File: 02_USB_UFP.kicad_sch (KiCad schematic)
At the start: 30 parts, among them U2 PI3USB302-Ax, U3 TUSB522Px, U4 TVS2200DRVx

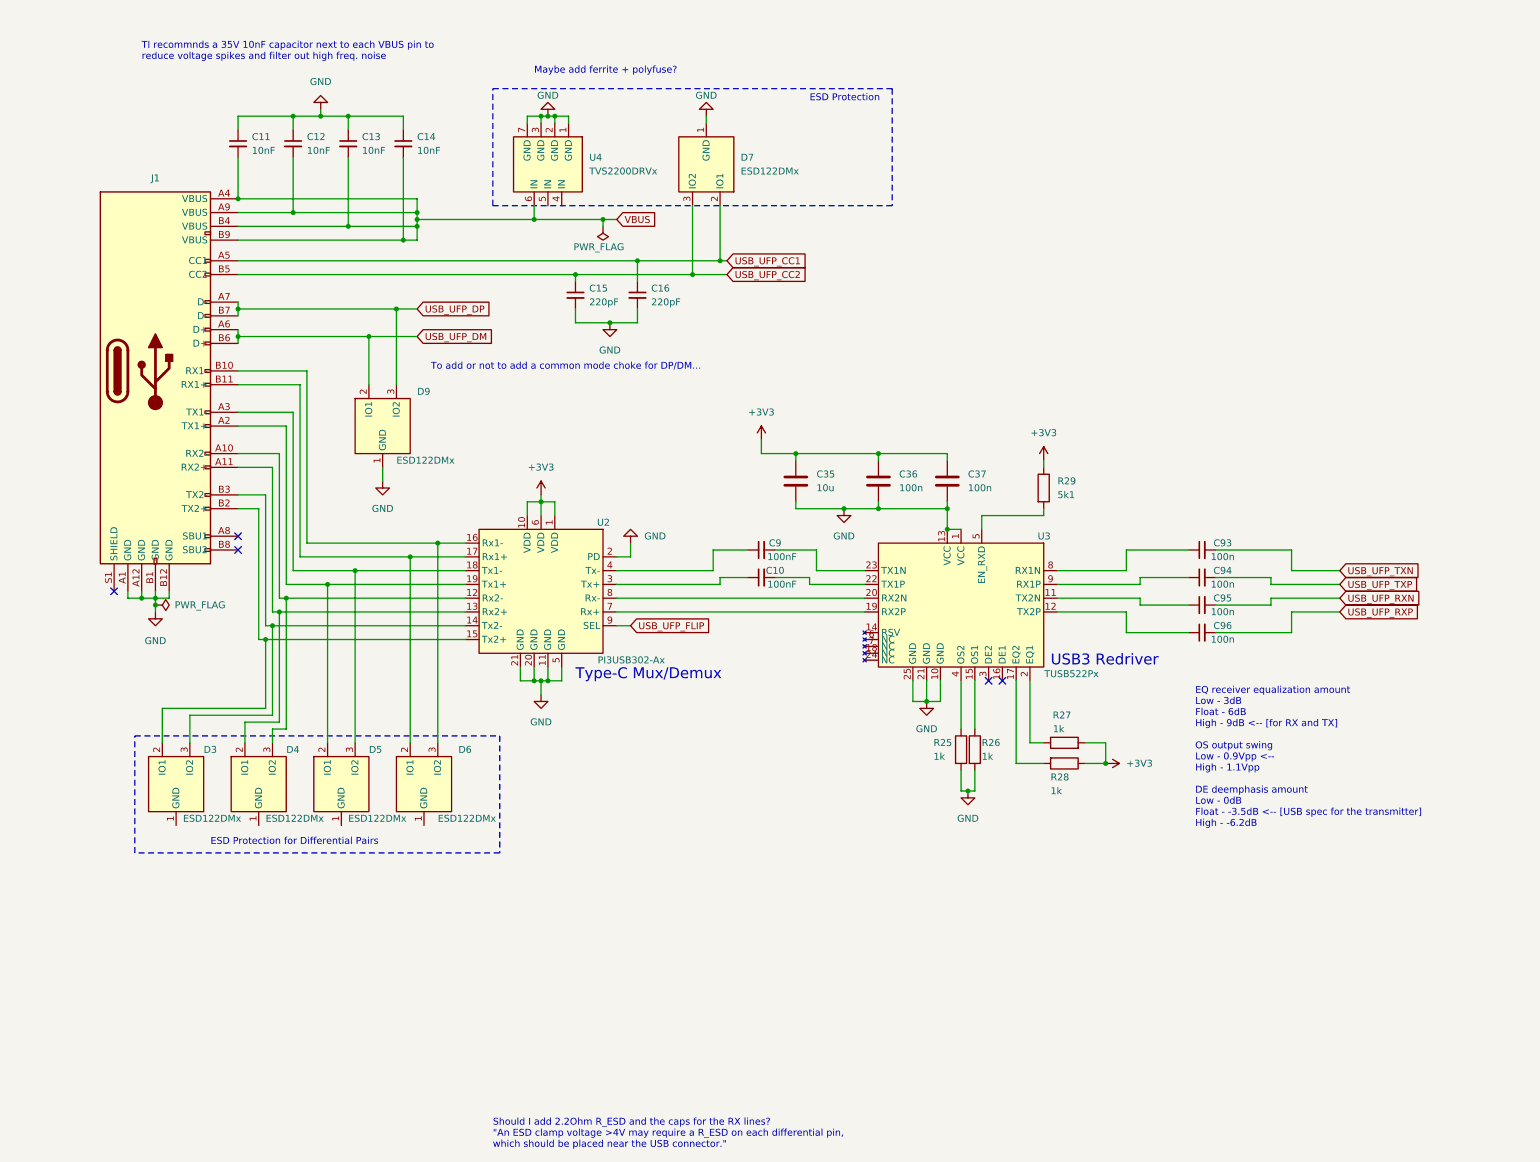
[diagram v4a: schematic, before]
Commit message: finish up schematics and ERC
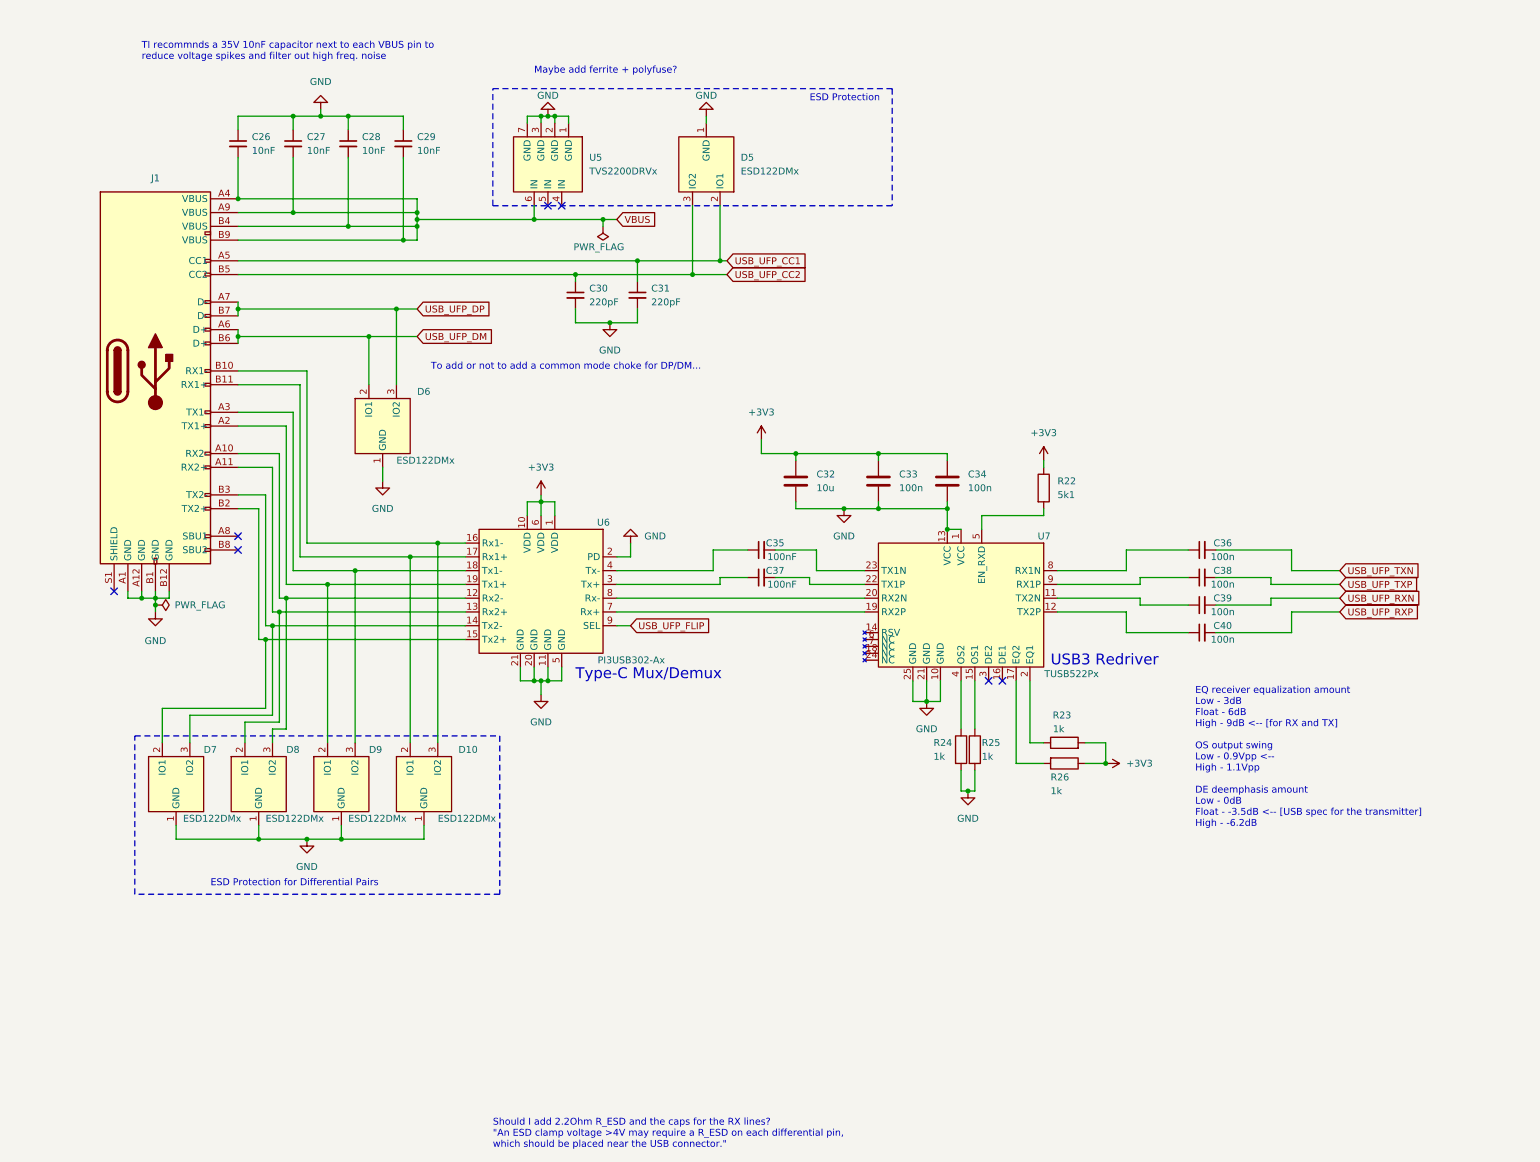
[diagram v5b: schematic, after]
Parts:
- renumbered C11 to C26, C12 to C27, C13 to C28, C14 to C29, C15 to C30, C16 to C31, C35 to C32, C36 to C33, C37 to C34, C9 to C35, C93 to C36, C10 to C37, C94 to C38, C95 to C39, C96 to C40, D6 to D10, D7 to D5, D9 to D6, D3 to D7, D4 to D8, D5 to D9, R29 to R22, R27 to R23, R25 to R24, R26 to R25, R28 to R26, U4 to U5, U2 to U6, U3 to U7
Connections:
- net GND: now also D10.1 (GND), D7.1 (GND), D8.1 (GND), D9.1 (GND)
- no-connect marks 5 -> 7

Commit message: finish setting footprints
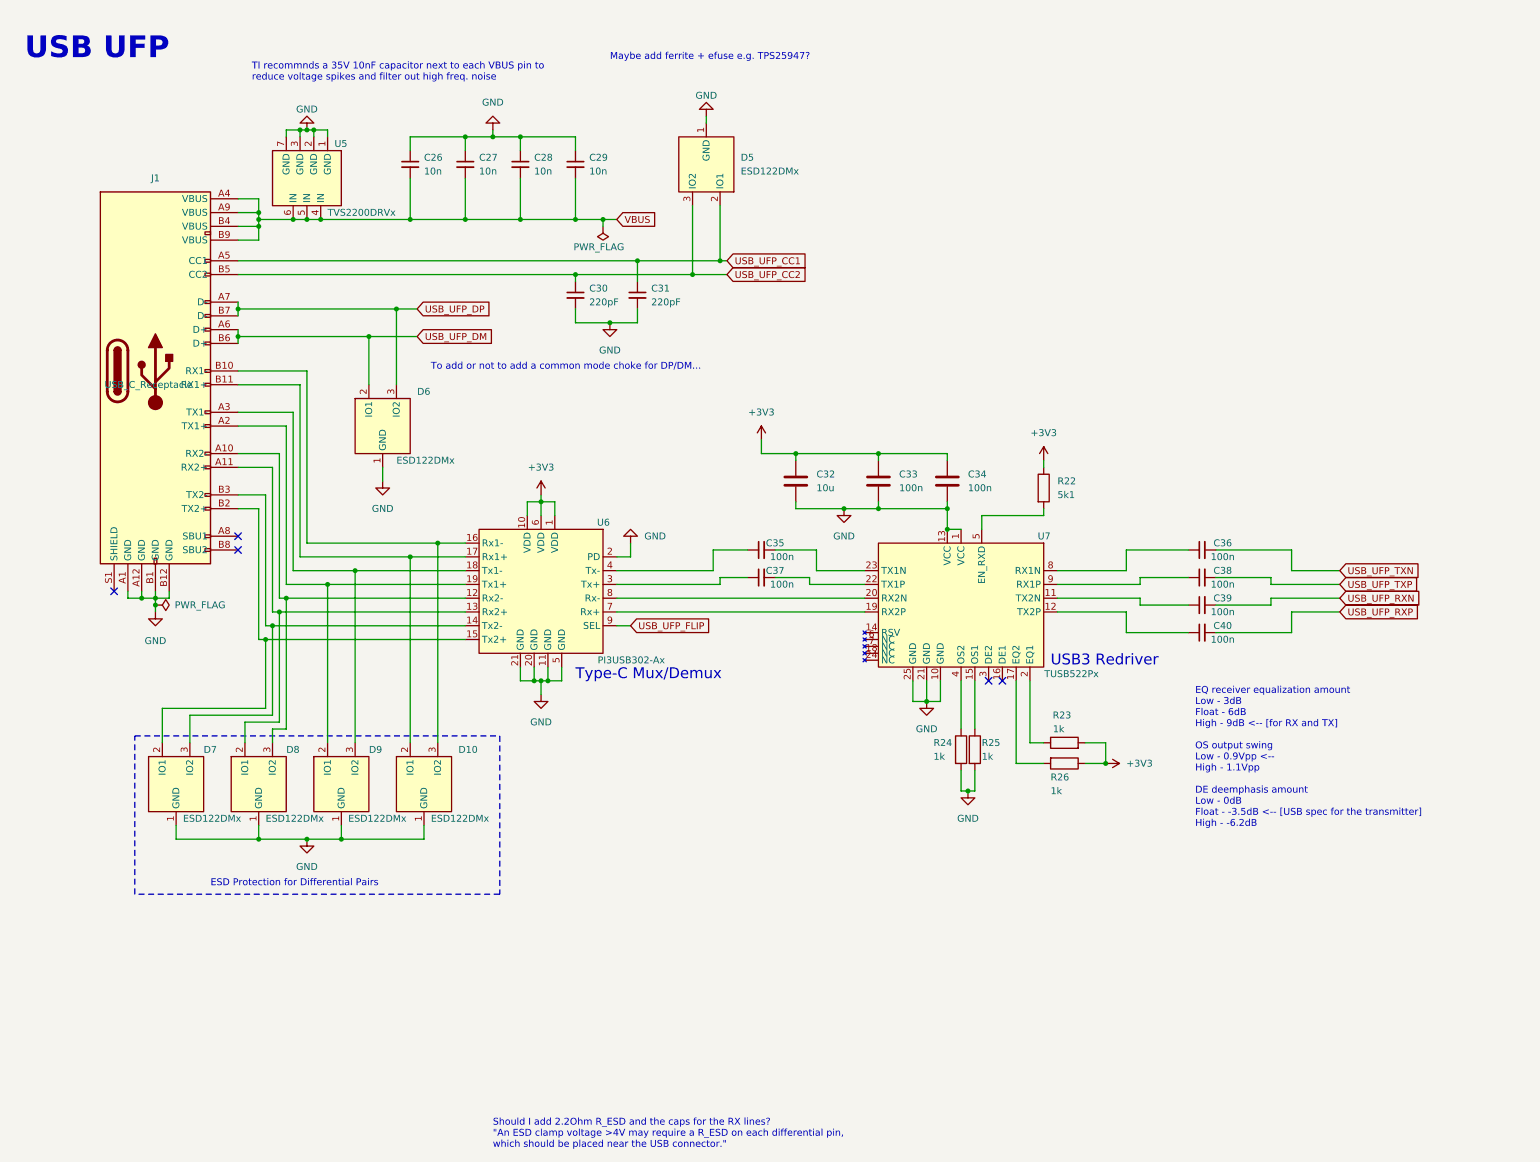
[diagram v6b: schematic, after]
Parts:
- C26, C27, C28, C29: value 10nF -> 10n; footprint (none) -> Capacitor_SMD:C_0603_1608Metric
- C30, C31, C32, C33, C34: footprint (none) -> Capacitor_SMD:C_0603_1608Metric
- C35, C37: value 100nF -> 100n; footprint (none) -> Capacitor_SMD:C_0402_1005Metric
- C36, C38, C39, C40: footprint (none) -> Capacitor_SMD:C_0402_1005Metric
- J1: value ~ -> USB_C_Receptacle; footprint (none) -> CakeUSB:USB_C_Receptacle_GT-USB-7052
- R22, R23, R24, R25, R26: footprint (none) -> Resistor_SMD:R_0603_1608Metric
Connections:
- net VBUS: now also U5.4 (IN), U5.5 (IN)
- no-connect marks 7 -> 5
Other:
- note added: "Maybe add ferrite + efuse e.g. TPS25947?"
- note added: "USB UFP"
- note removed: "ESD Protection"
- note removed: "Maybe add ferrite + polyfuse?"

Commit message: symbol fixes, switch ESD protection for USB datalines
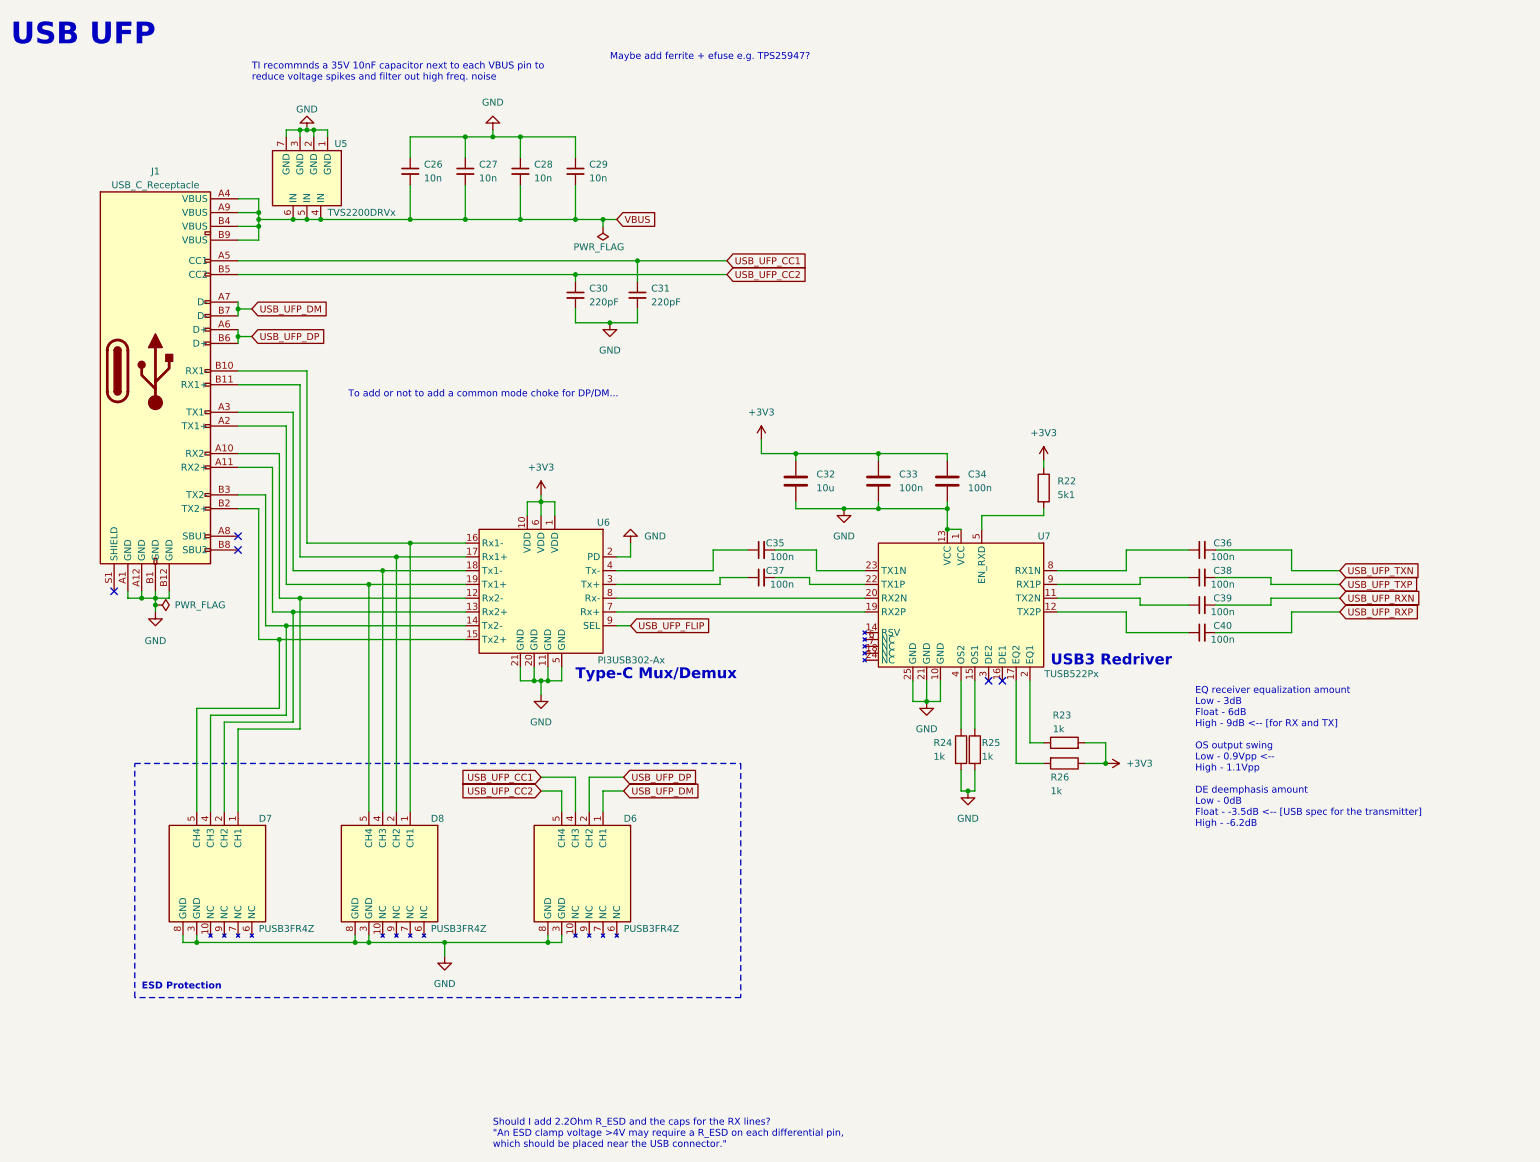
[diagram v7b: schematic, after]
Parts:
- removed D10, D5, D6, D7, D8, D9: ESD122DMx, Cake_USB:ESD122DMX, symbol CakeUSB:ESD122DMx
- added D6, D7, D8: PUSB3FR4Z, CakeUSB:PUSB3FR4Z, symbol CakeUSB:PUSB3FR4Z
- U5: footprint Cake_USB:TVS2200DRVx -> CakeUSB:TVS2200DRVx
- U6: footprint Cake_USB:PI3USB302-Ax -> CakeUSB:PI3USB302-Ax
- U7: footprint Cake_USB:TUSB522Px -> CakeUSB:TUSB522Px
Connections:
- net GND: now also D6.3 (GND), D6.8 (GND), D7.3 (GND), D7.8 (GND), D8.3 (GND), D8.8 (GND)
- net USB_UFP_CC1: now also D6.4 (CH3)
- net USB_UFP_CC2: now also D6.5 (CH4)
- net USB_UFP_DM: now also J1.A7 (D-), J1.B7 (D-), D6.1 (CH1); no longer J1.A6 (D+), J1.B6 (D+)
- net USB_UFP_DP: now also J1.A6 (D+), J1.B6 (D+), D6.2 (CH2); no longer J1.A7 (D-), J1.B7 (D-)
- net at J1.A2 (TX1+), U6.19 (Tx1+): now also D8.5 (CH4)
- net at J1.A3 (TX1-), U6.18 (Tx1-): now also D8.4 (CH3)
- net at J1.A10 (RX2-), U6.12 (Rx2-): now also D7.1 (CH1)
- net at J1.A11 (RX2+), U6.13 (Rx2+): now also D7.2 (CH2)
- net at J1.B3 (TX2-), U6.14 (Tx2-): now also D7.4 (CH3)
- net at J1.B2 (TX2+), U6.15 (Tx2+): now also D7.5 (CH4)
- net at J1.B10 (RX1-), U6.16 (Rx1-): now also D8.1 (CH1)
- net at J1.B11 (RX1+), U6.17 (Rx1+): now also D8.2 (CH2)
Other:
- note added: "ESD Protection"
- note removed: "ESD Protection for Differential Pairs"
- moved on the sheet: C26, C27, C28, C29
